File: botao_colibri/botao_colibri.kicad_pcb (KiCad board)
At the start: 2 copper layers, 79 x 137.8 mm, 0 parts

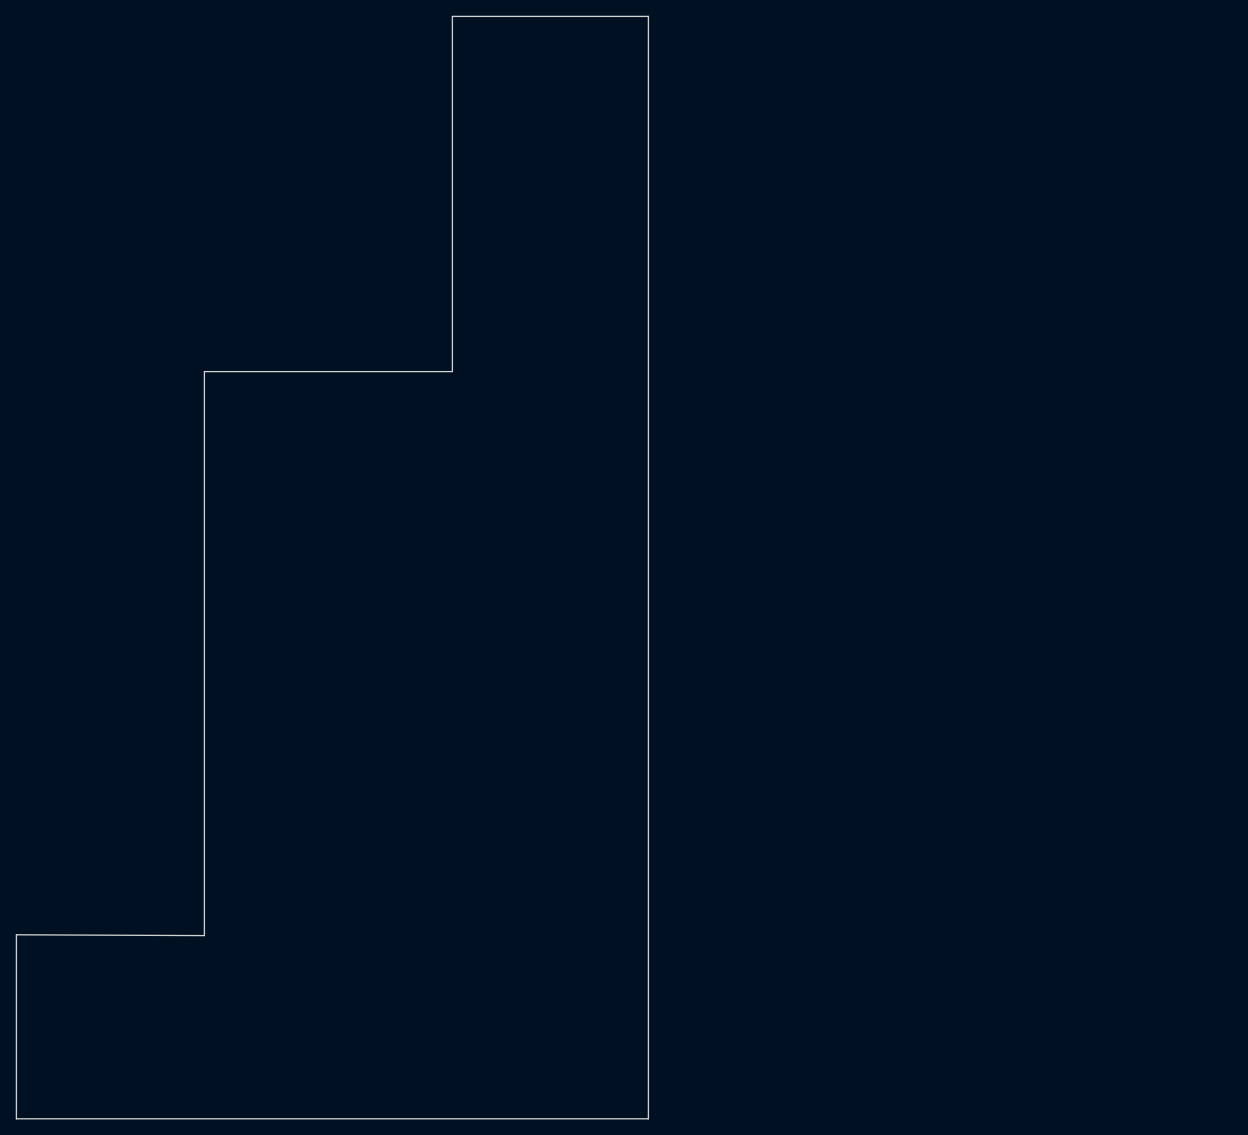
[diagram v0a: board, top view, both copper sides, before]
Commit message: chore: Update PCB/schematic edits and project files
Marks hole positions on the board, syncs KiCad project/prl files after
enabling the colibri-v4 library, and adds the botao_colibri KiCad
project files plus recent backup snapshots.

Co-Authored-By: Claude Sonnet 5 <noreply@anthropic.com>
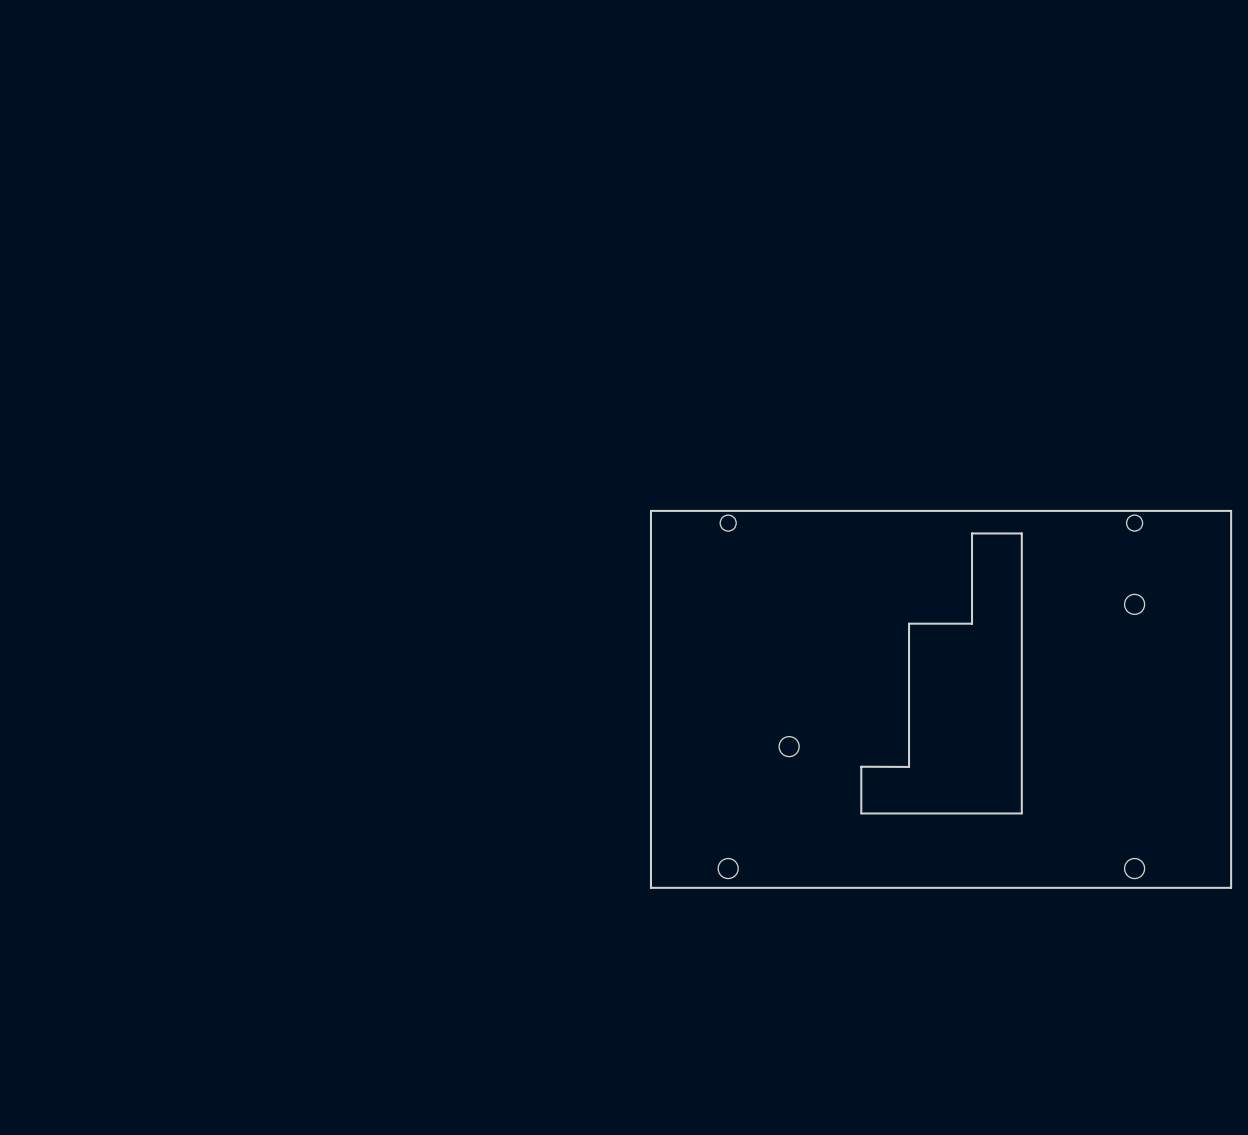
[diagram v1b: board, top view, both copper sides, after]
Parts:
- added H1: NPTH, NPTH, F.Cu at (139.8, 73.5)
- added H2: NPTH, NPTH, F.Cu at (89.0, 106.5)
- added H3: NPTH, NPTH, F.Cu at (139.8, 106.5)
- added H4: NPTH, NPTH, F.Cu at (96.6, 91.3)
- added H5: NPTH, NPTH, F.Cu at (89.0, 63.3)
- added H6: NPTH, NPTH, F.Cu at (139.8, 63.3)
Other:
- board size 79 x 137.8 mm -> 72.5 x 47.1 mm
